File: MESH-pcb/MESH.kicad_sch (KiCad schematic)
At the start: 32 parts, among them J1 Ant., J2 Conn_01x08_Pin, J3 Conn_01x08_Pin, J4 Conn_01x08_Pin, J5 Conn_01x08_Pin, J6 Conn_01x05_Pin, J7 USB_C_Receptacle_PowerOnly_6P, J8 Conn_01x02, Q1 SS8550, U1 STM32F070RBTx, U2 CC1101RTK, Y1 XTM32027000QT00351001, Y2 XTM32027000QT00351001

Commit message: Schematic update, PCB routing update
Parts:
- removed J7: USB_C_Receptacle_PowerOnly_6P, Connector_USB:USB_C_Receptacle_GCT_USB4125-xx-x_6P_TopMnt_Horizontal, symbol Connector:USB_C_Receptacle_PowerOnly_6P
- removed Q1: SS8550, Package_TO_SOT_SMD:SOT-23, symbol Transistor_BJT:SS8550
- removed U1: STM32F070RBTx, Package_QFP:LQFP-64_10x10mm_P0.5mm, symbol MCU_ST_STM32F0:STM32F070RBTx
- added C10, C11, C12, C9: 10nF, Capacitor_SMD:C_0402_1005Metric, symbol Device:C
- added C13, C14: 0.1uf, Capacitor_SMD:C_0402_1005Metric, symbol Device:C
- added D3, D4: LED, LED_SMD:LED_0603_1608Metric_Pad1.05x0.95mm_HandSolder, symbol Device:LED
- added J10: USB_C_Receptacle_USB2.0_16P, Connector_USB:USB_C_Receptacle_Palconn_UTC16-G, symbol Connector:USB_C_Receptacle_USB2.0_16P
- added J7: Conn_01x04_Pin, Connector_PinHeader_2.54mm:PinHeader_1x04_P2.54mm_Vertical, symbol Connector:Conn_01x04_Pin
- added J9: Conn_01x04_Pin, Connector_PinHeader_2.00mm:PinHeader_1x04_P2.00mm_Vertical, symbol Connector:Conn_01x04_Pin
- added Q2: AO3401A, Package_TO_SOT_SMD:SOT-23, symbol Transistor_FET:AO3401A
- added R10: 56k, Capacitor_SMD:C_0201_0603Metric_Pad0.64x0.40mm_HandSolder, symbol Device:R
- added R11, R12: 220, Resistor_SMD:R_0201_0603Metric_Pad0.64x0.40mm_HandSolder, symbol Device:R
- added R13: 1k, Resistor_SMD:R_0201_0603Metric_Pad0.64x0.40mm_HandSolder, symbol Device:R
- added R6, R7: 10k, Resistor_SMD:R_0201_0603Metric_Pad0.64x0.40mm_HandSolder, symbol Device:R
- added R8, R9: 5.1k, Resistor_SMD:R_0201_0603Metric_Pad0.64x0.40mm_HandSolder, symbol Device:R
- added SW1, SW2: SW_Push, custom:SW_5.6_3.1, symbol Switch:SW_Push
- added U4: AP2127R-3.3, Package_TO_SOT_SMD:SOT-89-3, symbol Regulator_Linear:AP2127R-3.3
- added U5: STM32L053R8Tx, Package_QFP:LQFP-64_10x10mm_P0.5mm, symbol MCU_ST_STM32L0:STM32L053R8Tx
- R1: footprint (none) -> Capacitor_SMD:C_0201_0603Metric_Pad0.64x0.40mm_HandSolder
- R2: value 1k -> 220
- U2: footprint additional:QFN50P350X350X100-21N -> Package_DFN_QFN:QFN-20-1EP_4x4mm_P0.5mm_EP2.5x2.5mm
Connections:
- net GDO0: now also U5.3 (PC14)
- net GDO2: now also U5.4 (PC15)
- net GND: now also C10.2, C11.2, C12.2, C13.2, C14.2, C9.2, D3.1 (K), D4.1 (K), J10.A1 (GND), J10.A12 (GND), J10.B1 (GND), J10.B12 (GND), J10.S1 (SHIELD), J7.1 (Pin_1), J9.4 (Pin_4), R7.2, R8.2, R9.2, SW1.1, SW2.1, U4.1 (GND), U5.12 (VSSA), U5.18 (VSS), U5.31 (VSS), U5.47 (VSS), U5.63 (VSS)
- net I2C1_SCL: now also U5.58 (PB6)
- net I2C1_SDA: now also U5.59 (PB7)
- net MISO: now also U5.22 (PA6)
- net MOSI: now also U5.23 (PA7)
- net RX2: now also U5.17 (PA3)
- net SCK: now also U5.21 (PA5)
- net TX2: now also U5.16 (PA2)
- net USB_DM: now also J10.A7 (D-), J10.B7 (D-), U5.44 (PA11)
- net USB_DP: now also J10.A6 (D+), J10.B6 (D+), U5.45 (PA12)
- net VCC: now also C10.1, C11.1, C12.1, C9.1, J7.4 (Pin_4), Q2.2 (S), R10.1, R13.2, U4.3 (VO), U5.1 (VLCD), U5.13 (VDDA), U5.19 (VDD), U5.32 (VDD), U5.48 (VDD_USB), U5.64 (VDD)
- net charger/BAT: now also R6.1, U4.2 (VI)
- net charger/Vcc: now also J10.A4 (VBUS), J10.A9 (VBUS), J10.B4 (VBUS), J10.B9 (VBUS)
- net at C2.2, Y2.1: now also U5.5 (PH0)
- net at C3.1, Y2.3: now also U5.6 (PH1)
- net at J4.3 (Pin_3): now also U5.57 (PB5)
- net at J4.4 (Pin_4): now also U5.56 (PB4)
- net at J4.5 (Pin_5): now also U5.55 (PB3)
- net at J4.6 (Pin_6): now also U5.28 (PB2)
- net at J4.7 (Pin_7): now also U5.27 (PB1)
- net at J4.8 (Pin_8): now also U5.26 (PB0)
- net at JP1.3 (B): now also U5.20 (PA4)
- net at J2.3 (Pin_3): now also U5.10 (PC2)
- net at J2.4 (Pin_4): now also U5.11 (PC3)
- net at J3.6 (Pin_6): now also U5.2 (PC13)
- net at J2.5 (Pin_5): now also U5.24 (PC4)
- net at J2.6 (Pin_6): now also U5.25 (PC5)
- net at J5.6 (Pin_6): now also U5.29 (PB10)
- net at J5.5 (Pin_5): now also U5.30 (PB11)
- net at J5.4 (Pin_4): now also U5.33 (PB12)
- net at J5.3 (Pin_3): now also U5.34 (PB13)
- net at J5.2 (Pin_2): now also U5.35 (PB14)
- net at J5.1 (Pin_1): now also U5.36 (PB15)
- net at J2.7 (Pin_7): now also U5.37 (PC6)
- net at J2.8 (Pin_8): now also U5.38 (PC7)
- net at J3.1 (Pin_1): now also U5.39 (PC8)
- net at J3.2 (Pin_2): now also U5.40 (PC9)
- net at J3.3 (Pin_3): now also U5.51 (PC10)
- net at J3.4 (Pin_4): now also U5.52 (PC11)
- net at J3.5 (Pin_5): now also U5.53 (PC12)
- net at J5.8 (Pin_8): now also U5.61 (PB8)
- net at J5.7 (Pin_7): now also U5.62 (PB9)
- net at J2.1 (Pin_1): now also U5.8 (PC0)
- net at J2.2 (Pin_2): now also U5.9 (PC1)
- net at R2.1: now also Q2.1 (G), R13.1
- net at J6.5 (Pin_5): now also J9.1 (Pin_1), Q2.3 (D)
- new net: J10.A5 (CC1), R8.1
- new net: J10.B5 (CC2), R9.1
- new net: D4.2 (A), R12.2
- new net: C13.1, SW1.2, U5.60 (BOOT0)
- new net: D3.2 (A), R11.2
- new net BAT_V: R6.2, R7.1, U5.14 (PA0)
- new net LED1: R11.1, U5.50 (PA15)
- new net LED2: R12.1, U5.15 (PA1)
- new net SWCLK: J7.2 (Pin_2), U5.49 (PA14)
- new net SWDIO: J7.3 (Pin_3), U5.46 (PA13)
- new net USR_BTN: C14.1, R10.2, SW2.2, U5.43 (PA10)
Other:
- moved on the sheet: C1, C121, C122, C123, C124, C125, C131, C2, C3, C4, C7, C8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

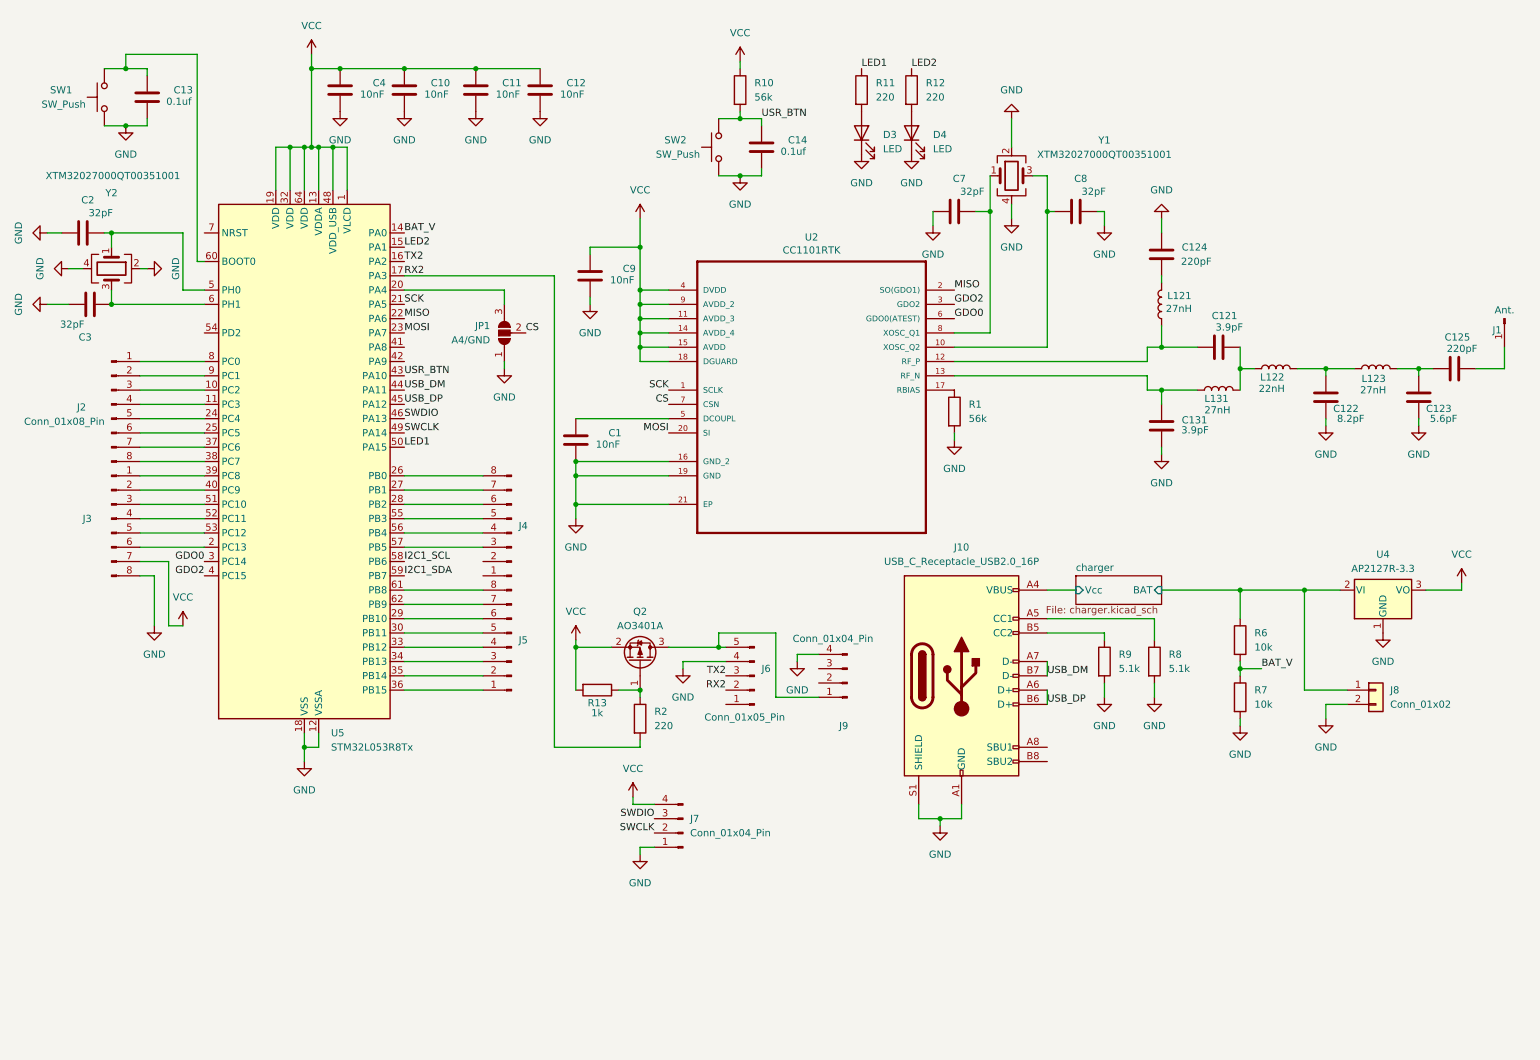
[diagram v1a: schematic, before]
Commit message: Added custom component library, Almost final component placement
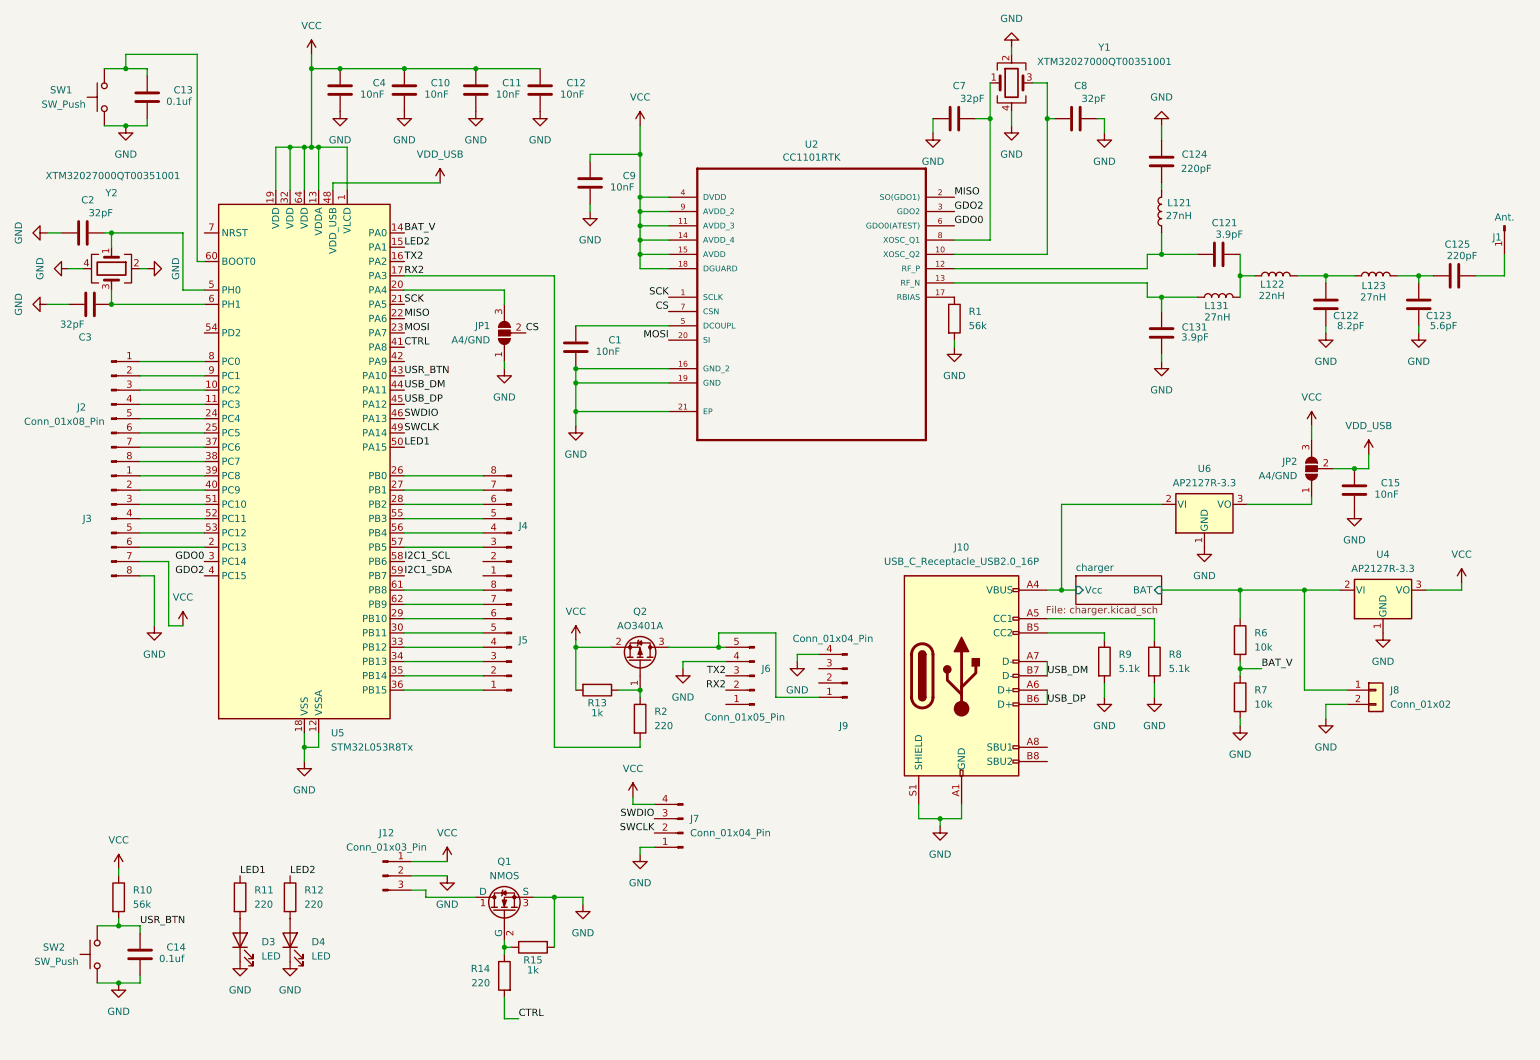
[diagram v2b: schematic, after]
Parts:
- added C15: 10nF, Capacitor_SMD:C_0402_1005Metric, symbol Device:C
- added J12: Conn_01x03_Pin, Connector_PinSocket_2.54mm:PinSocket_1x03_P2.54mm_Vertical, symbol Connector:Conn_01x03_Pin
- added JP2: A4/GND, Jumper:SolderJumper-3_P2.0mm_Open_TrianglePad1.0x1.5mm_NumberLabels, symbol Jumper:SolderJumper_3_Open
- added Q1: NMOS, lib:SOIC127P600X175-8N, symbol Simulation_SPICE:NMOS
- added R14: 220, Resistor_SMD:R_0201_0603Metric_Pad0.64x0.40mm_HandSolder, symbol Device:R
- added R15: 1k, Resistor_SMD:R_0201_0603Metric_Pad0.64x0.40mm_HandSolder, symbol Device:R
- added U6: AP2127R-3.3, Package_TO_SOT_SMD:SOT-89-3, symbol Regulator_Linear:AP2127R-3.3
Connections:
- net GND: now also C15.2, J12.2 (Pin_2), Q1.3 (S), R15.2, U6.1 (GND)
- net VCC: now also J12.1 (Pin_1), JP2.3 (B); no longer U5.48 (VDD_USB)
- net charger/Vcc: now also U6.2 (VI)
- net CTRL: now reaches U5.41 (PA8)
- net CTRL: now also R14.2
- new net: JP2.1 (A), U6.3 (VO)
- new net: J12.3 (Pin_3), Q1.1 (D)
- new net: Q1.2 (G), R14.1, R15.1
- new net VDD_USB: C15.1, JP2.2 (C), U5.48 (VDD_USB)
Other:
- moved on the sheet: C1, C121, C122, C123, C124, C125, C131, C14, C7, C8, C9, D3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

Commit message: routing almost complete
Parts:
- removed J7: Conn_01x04_Pin, Connector_PinHeader_2.54mm:PinHeader_1x04_P2.54mm_Vertical, symbol Connector:Conn_01x04_Pin
- added J11: Conn_01x02_Pin, Connector_PinHeader_2.54mm:PinHeader_1x02_P2.54mm_Vertical, symbol Connector:Conn_01x02_Pin
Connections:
- net I2C1_SCL is gone; now on an unnamed net: U5.58 (PB6)
- net I2C1_SDA is gone; now on an unnamed net: U5.59 (PB7)
- net GND: now also J11.1 (Pin_1); no longer J3.8 (Pin_8)
- net RX2: no longer R2.2
- net SWCLK: now also J3.7 (Pin_7)
- net SWDIO: now also J3.8 (Pin_8)
- net VCC: now also J11.2 (Pin_2); no longer J3.7 (Pin_7)
- net at U5.42 (PA9): now also R2.2
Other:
- moved on the sheet: J3

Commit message: Ready to be exported
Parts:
- removed U4, U6: AP2127R-3.3, Package_TO_SOT_SMD:SOT-89-3, symbol Regulator_Linear:AP2127R-3.3
- added Q3: NMOS, lib:SOIC127P600X175-8N, symbol Simulation_SPICE:NMOS
- added R16: 220, Resistor_SMD:R_0201_0603Metric_Pad0.64x0.40mm_HandSolder, symbol Device:R
- added R17: 1k, Resistor_SMD:R_0201_0603Metric_Pad0.64x0.40mm_HandSolder, symbol Device:R
- added U3, U4: AP2127K-3.3, Package_TO_SOT_SMD:SOT-23-5, symbol Regulator_Linear:AP2127K-3.3
- R1, R10: footprint Capacitor_SMD:C_0201_0603Metric_Pad0.64x0.40mm_HandSolder -> Resistor_SMD:R_0201_0603Metric_Pad0.64x0.40mm_HandSolder
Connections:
- net GND: now also J12.1 (Pin_1), Q3.3 (S), R17.2, U3.2 (GND), U4.2 (GND); no longer J12.2 (Pin_2)
- net VCC: now also U4.5 (VOUT); no longer J12.1 (Pin_1)
- net charger/BAT: now also U4.1 (VIN)
- net charger/Vcc: now also U3.1 (VIN)
- net at JP2.1 (A): now also U3.5 (VOUT)
- net at J4.8 (Pin_8): no longer U5.26 (PB0)
- net CTRL renamed CTRL1
- new net: Q3.2 (G), R16.1, R17.1
- new net: J12.2 (Pin_2), Q3.1 (D)
- new net CTRL2: R16.2, U5.26 (PB0)
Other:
- moved on the sheet: J11, J12, Q1, R14, R15

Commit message: added pinheader footprint without outline, added pin names to silkscreen
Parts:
- J2, J3, J4, J5: footprint Connector_PinHeader_2.54mm:PinHeader_1x08_P2.54mm_Vertical -> lib:PinHeader_1x08_P2.54mm_Bare
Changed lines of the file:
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@@
 			)
 		)
-		(property "Footprint" "Connector_PinHeader_2.54mm:PinHeader_1x08_P2.54mm_Vertical"
+		(property "Footprint" "lib:PinHeader_1x08_P2.54mm_Bare"
 			(at 101.6 105.41 0)
 			(effects
@@
 			)
 		)
-		(property "Footprint" "Connector_PinHeader_2.54mm:PinHeader_1x08_P2.54mm_Vertical"
+		(property "Footprint" "lib:PinHeader_1x08_P2.54mm_Bare"
 			(at 30.48 82.55 0)
 			(effects
@@
 			)
 		)
-		(property "Footprint" "Connector_PinHeader_2.54mm:PinHeader_1x08_P2.54mm_Vertical"
+		(property "Footprint" "lib:PinHeader_1x08_P2.54mm_Bare"
 			(at 101.6 125.73 0)
 			(effects
@@
 			)
 		)
-		(property "Footprint" "Connector_PinHeader_2.54mm:PinHeader_1x08_P2.54mm_Vertical"
+		(property "Footprint" "lib:PinHeader_1x08_P2.54mm_Bare"
 			(at 22.86 102.87 0)
 			(effects

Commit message: Added all pin names
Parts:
- J11: footprint Connector_PinHeader_2.54mm:PinHeader_1x02_P2.54mm_Vertical -> lib:PinHeader_1x02_P2.54mm_Bare
- J12: footprint Connector_PinSocket_2.54mm:PinSocket_1x03_P2.54mm_Vertical -> lib:PinHeader_1x03_P2.54mm_Bare
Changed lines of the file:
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@@
 			)
 		)
-		(property "Footprint" "Connector_PinSocket_2.54mm:PinSocket_1x03_P2.54mm_Vertical"
+		(property "Footprint" "lib:PinHeader_1x03_P2.54mm_Bare"
 			(at 78.74 160.02 0)
 			(effects
@@
 			)
 		)
-		(property "Footprint" "Connector_PinHeader_2.54mm:PinHeader_1x02_P2.54mm_Vertical"
+		(property "Footprint" "lib:PinHeader_1x02_P2.54mm_Bare"
 			(at 153.67 156.21 0)
 			(effects
